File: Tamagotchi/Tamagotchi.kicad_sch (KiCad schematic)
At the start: 1 part, among them U1 XIAO-ESP32-C6-DIP

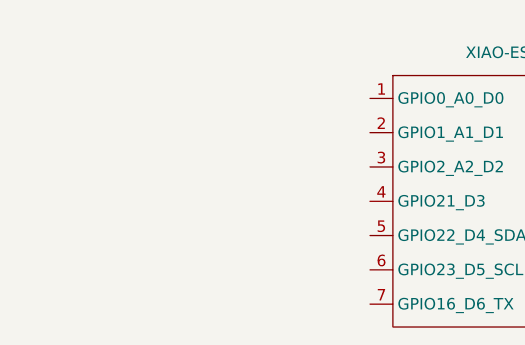
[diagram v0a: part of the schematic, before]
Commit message: finally found a oled
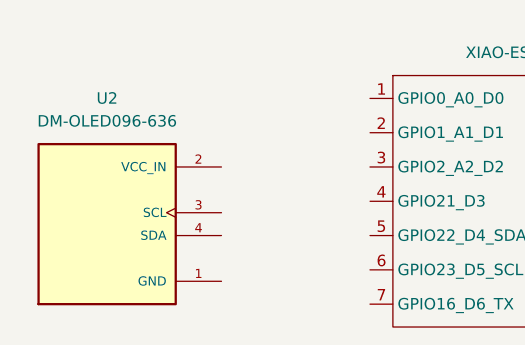
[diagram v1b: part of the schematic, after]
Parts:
- added U2: DM-OLED096-636, DM-OLED096-636:MODULE_DM-OLED096-636, symbol DM-OLED096-636:DM-OLED096-636
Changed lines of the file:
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@@
 	(paper "A4")
+	(symbol
+		(lib_id "DM-OLED096-636:DM-OLED096-636")
+		(at 100.33 95.25 0)
+		(unit 1)
+		(body_style 1)
+		(exclude_from_sim no)
+		(in_bom yes)
+		(on_board yes)
+		(in_pos_files yes)
+		(dnp no)
+		(fields_autoplaced yes)
+		(property "Reference" "U2"
+			(at 100.33 80.01 0)
+			(show_name no)
+			(do_not_autoplace no)
+			(effects
+				(font
+					(size 1.27 1.27)
+				)
+			)
+		)
+		(property "Value" "DM-OLED096-636"
+			(at 100.33 82.55 0)
+			(show_name no)
+			(do_not_autoplace no)
+			(effects
+				(font
+					(size 1.27 1.27)
+				)
+			)
+		)
+		(property "Footprint" "DM-OLED096-636:MODULE_DM-OLED096-636"
+			(at 100.33 95.25 0)
+			(hide yes)
+			(show_name no)
+			(do_not_autoplace no)
+			(effects
+				(font
+					(size 1.27 1.27)
+				)
+				(justify bottom)
+			)
+		)
+		(property "Datasheet" ""
+			(at 100.33 95.25 0)
+			(hide yes)
+			(show_name no)
+			(do_not_autoplace no)
+			(effects
+				(font
+					(size 1.27 1.27)
+				)
+			)
+		)
+		(property "Description" "0.96” 128 X 64 MONOCHROME GRAPHIC OLED DISPLAY MODULE - I2C"
+			(at 100.33 95.25 0)
+			(hide yes)
+			(show_name no)
+			(do_not_autoplace no)
+			(effects
+				(font
+					(size 1.27 1.27)
+				)
+				(justify bottom)
+			)
+		)
+		(property "MF" "Display Module"
+			(at 100.33 95.25 0)
+			(hide yes)
+			(show_name no)
+			(do_not_autoplace no)
+			(effects
+				(font
+					(size 1.27 1.27)
+				)
+				(justify bottom)
+			)
+		)
+		(property "MAXIMUM_PACKAGE_HEIGHT" "11.3 mm"
+			(at 100.33 95.25 0)
+			(hide yes)
+			(show_name no)
+			(do_not_autoplace no)
+			(effects
+				(font
+					(size 1.27 1.27)
+				)
+				(justify bottom)
+			)
+		)
+		(property "Package" "Package"
+			(at 100.33 95.25 0)
+			(hide yes)
+			(show_name no)
+			(do_not_autoplace no)
+			(effects
+				(font
+					(size 1.27 1.27)
+				)
+				(justify bottom)
+			)
+		)
+		(property "Price" "None"
+			(at 100.33 95.25 0)
+			(hide yes)
+			(show_name no)
+			(do_not_autoplace no)
+			(effects
+				(font
+					(size 1.27 1.27)
+				)
+				(justify bottom)
+			)
+		)
+		(property "Check_prices" "https://www.snapeda.com/parts/DM-OLED096-636/Display+Module/view-part/?ref=eda"
+			(at 100.33 95.25 0)
+			(hide yes)
+			(show_name no)
+			(do_not_autoplace no)
+			(effects
+				(font
+					(size 1.27 1.27)
+				)
+				(justify bottom)
+			)
+		)
+		(property "STANDARD" "Manufacturer Recommendations"
+			(at 100.33 95.25 0)
+			(hide yes)
+			(show_name no)
+			(do_not_autoplace no)
+			(effects
+				(font
+					(size 1.27 1.27)
+				)
+				(justify bottom)
+			)
+		)
+		(property "PARTREV" "2018-09-10"
+			(at 100.33 95.25 0)
+			(hide yes)
+			(show_name no)
+			(do_not_autoplace no)
+			(effects
+				(font
+					(size 1.27 1.27)
+				)
+				(justify bottom)
+			)
+		)
+		(property "SnapEDA_Link" "https://www.snapeda.com/parts/DM-OLED096-636/Display+Module/view-part/?ref=snap"
+			(at 100.33 95.25 0)
+			(hide yes)
+			(show_name no)
+			(do_not_autoplace no)
+			(effects
+				(font
+					(size 1.27 1.27)
+				)
+				(justify bottom)
+			)
+		)
+		(property "MP" "DM-OLED096-636"
+			(at 100.33 95.25 0)
+			(hide yes)
+			(show_name no)
+			(do_not_autoplace no)
+			(effects
+				(font
+					(size 1.27 1.27)
+				)
+				(justify bottom)
+			)
+		)
+		(property "Availability" "Not in stock"
+			(at 100.33 95.25 0)
+			(hide yes)
+			(show_name no)
+			(do_not_autoplace no)
+			(effects
+				(font
+					(size 1.27 1.27)
+				)
+				(justify bottom)
+			)
+		)
+		(property "MANUFACTURER" "Displaymodule"
+			(at 100.33 95.25 0)
+			(hide yes)
+			(show_name no)
+			(do_not_autoplace no)
+			(effects
+				(font
+					(size 1.27 1.27)
+				)
+				(justify bottom)
+			)
+		)
+		(pin "4"
+		)
+		(pin "3"
+		)
+		(pin "1"
+		)
+		(pin "2"
+		)
+		(instances
+			(project "Tamagotchi"
+				(path "/dd5d29a8-0ca1-4c75-a105-470d6b907a46"
+					(reference "U2")
+					(unit 1)
+				)
+			)
+		)
+	)
 	(symbol
 		(lib_id "Seeed_Studio_XIAO_Series:XIAO-ESP32-C6-DIP")

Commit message: finished the schematic
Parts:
- added D1, D2, D3: LED, LED_THT:LED_D1.8mm_W1.8mm_H2.4mm_Horizontal_O1.27mm_Z4.9mm, symbol Device:LED
- added SW1, SW2, SW3: SW_Push, Button_Switch_THT:KSA_Tactile_SPST, symbol Switch:SW_Push
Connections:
- net GND: now reaches U2.1 (GND)
- net GND: now also U1.13 (GND), D1.1 (K), D2.1 (K), D3.1 (K), SW1.1, SW2.1, SW3.1
- net +3V3: now reaches U2.2 (VCC_IN)
- net +3V3: now also U1.12 (3V3)
- net at U2.3 (SCL): now also U1.6 (GPIO23_D5_SCL)
- net at U2.4 (SDA): now also U1.5 (GPIO22_D4_SDA)
- net at U1.1 (GPIO0_A0_D0): now also SW1.2
- net +5V: now reaches U1.14 (VBUS)
- net at U1.2 (GPIO1_A1_D1): now also SW2.2
- net at U1.3 (GPIO2_A2_D2): now also SW3.2
- net at U1.4 (GPIO21_D3): now also D1.2 (A)
- net at U1.7 (GPIO16_D6_TX): now also D3.2 (A)
- net at U1.8 (GPIO17_D7_RX): now also D2.2 (A)

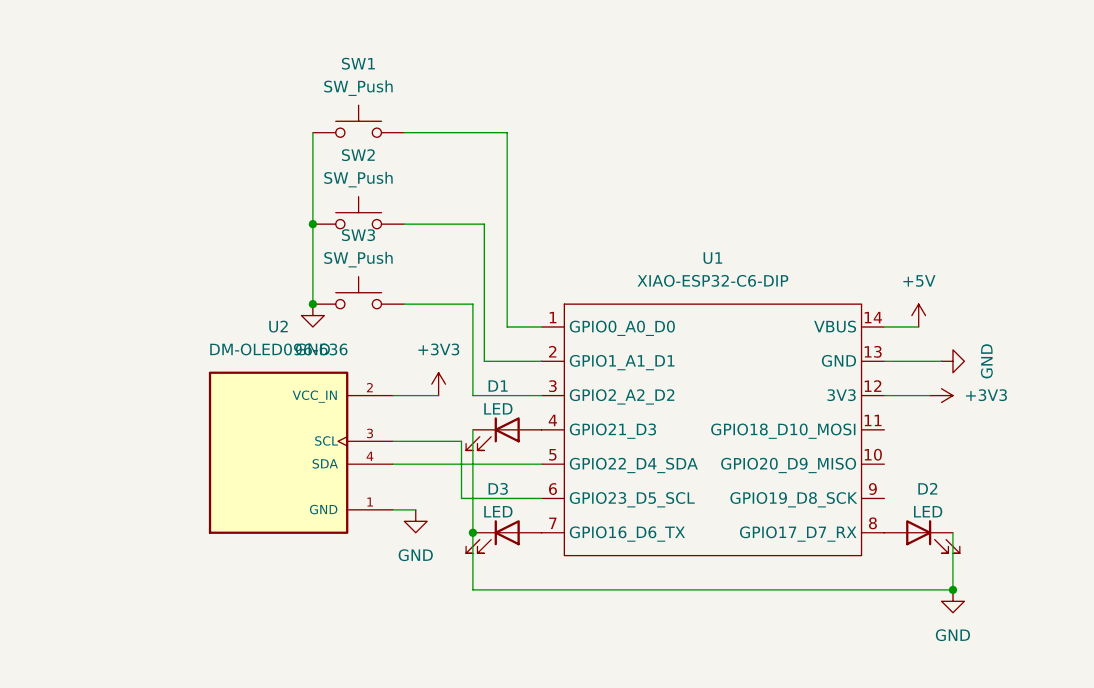
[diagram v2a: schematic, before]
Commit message: trying to fix my errors in schematic
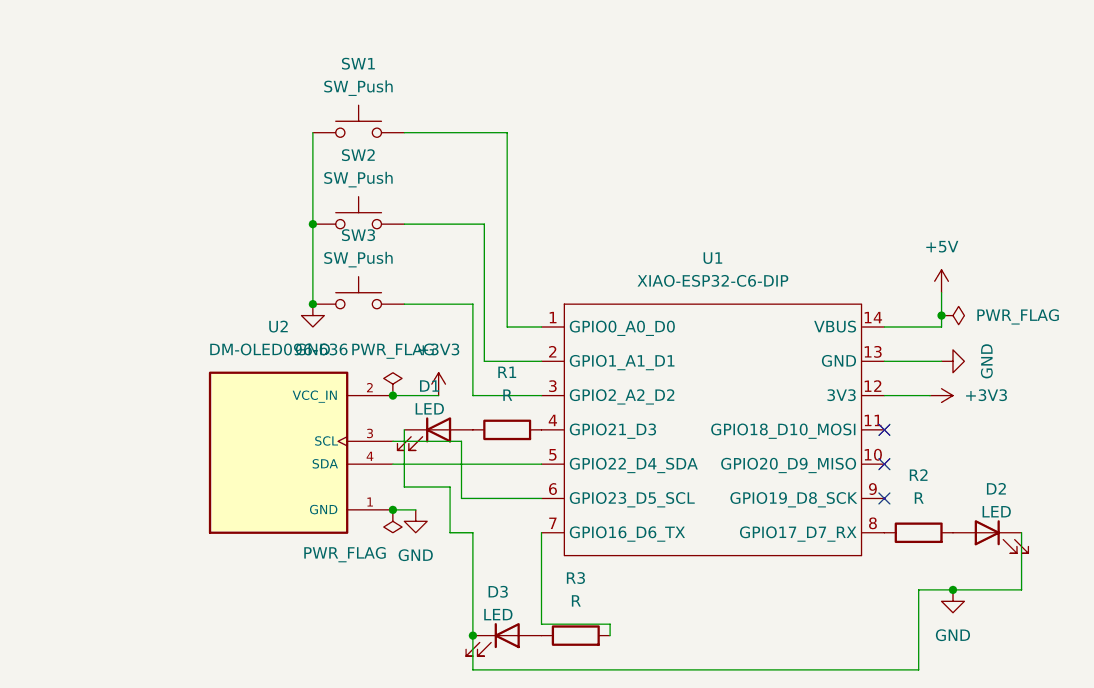
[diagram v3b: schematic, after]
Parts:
- added R1, R2, R3: R, symbol Device:R
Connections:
- net at D1.2 (A): now also R1.1; no longer U1.4 (GPIO21_D3)
- net at D3.2 (A): now also R3.1; no longer U1.7 (GPIO16_D6_TX)
- net at U1.8 (GPIO17_D7_RX): now also R2.1; no longer D2.2 (A)
- new net: R3.2, U1.7 (GPIO16_D6_TX)
- new net: R1.2, U1.4 (GPIO21_D3)
- new net: D2.2 (A), R2.2
- no-connect marks 0 -> 3
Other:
- moved on the sheet: D1, D2, D3

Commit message: spend so much time finding footprints
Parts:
- R1, R2, R3: footprint (none) -> Resistor_THT:R_Axial_DIN0204_L3.6mm_D1.6mm_P5.08mm_Horizontal
- U1: footprint Seeed_Studio_XIAO_Series:XIAO-ESP32-C6-DIP -> Seeed Studio XIAO Series Library:XIAO-ESP32-C6-DIP
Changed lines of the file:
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@@
 			)
 		)
-		(property "Footprint" ""
+		(property "Footprint" "Resistor_THT:R_Axial_DIN0204_L3.6mm_D1.6mm_P5.08mm_Horizontal"
 			(at 133.35 116.078 90)
 			(hide yes)
@@
 			)
 		)
-		(property "Footprint" ""
+		(property "Footprint" "Resistor_THT:R_Axial_DIN0204_L3.6mm_D1.6mm_P5.08mm_Horizontal"
 			(at 125.73 93.218 90)
 			(hide yes)
@@
 			)
 		)
-		(property "Footprint" "Seeed_Studio_XIAO_Series:XIAO-ESP32-C6-DIP"
+		(property "Footprint" "Seeed Studio XIAO Series Library:XIAO-ESP32-C6-DIP"
 			(at 149.86 86.36 0)
 			(hide yes)
@@
 			)
 		)
-		(property "Footprint" ""
+		(property "Footprint" "Resistor_THT:R_Axial_DIN0204_L3.6mm_D1.6mm_P5.08mm_Horizontal"
 			(at 171.45 104.648 90)
 			(hide yes)

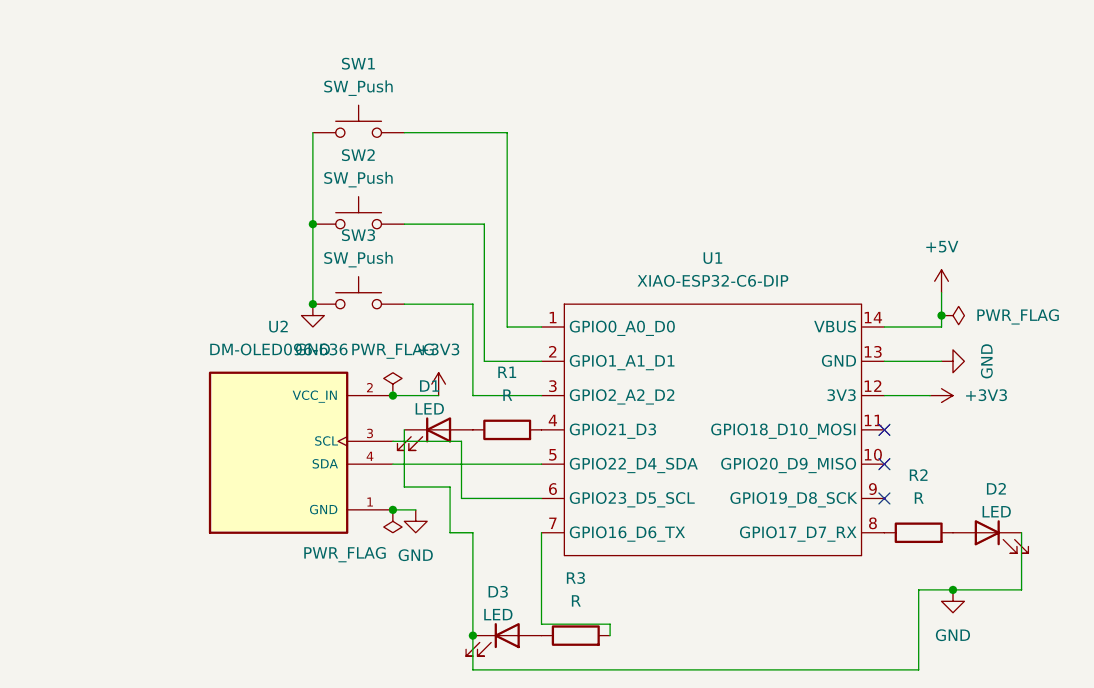
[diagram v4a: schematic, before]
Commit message: added some resistor and capacitors
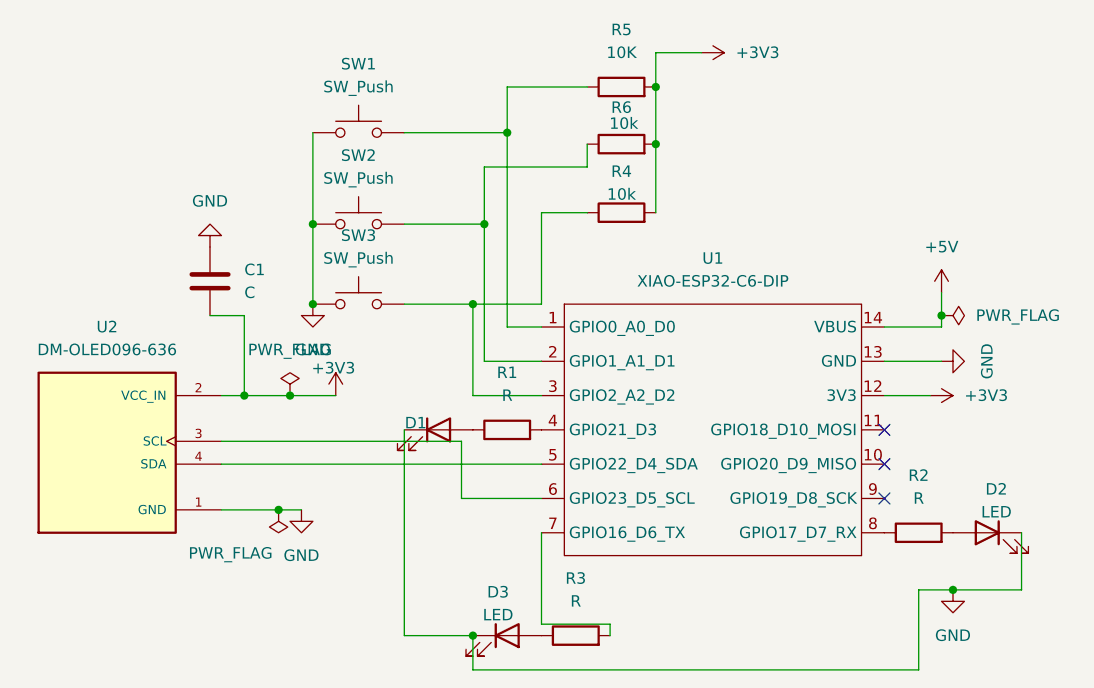
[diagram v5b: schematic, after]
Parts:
- added C1: C, Capacitor_SMD:C_0805_2012Metric, symbol Device:C
- added R4, R6: 10k, Resistor_SMD:R_0805_2012Metric, symbol Device:R
- added R5: 10K, Resistor_SMD:R_0805_2012Metric, symbol Device:R
- R1, R2, R3: footprint Resistor_THT:R_Axial_DIN0204_L3.6mm_D1.6mm_P5.08mm_Horizontal -> Resistor_SMD:R_0805_2012Metric
- U2: footprint DM-OLED096-636:MODULE_DM-OLED096-636 -> DM-OLED096-636 (1):MODULE_DM-OLED096-636
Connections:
- net +3V3: now also C1.1, R4.2, R5.2, R6.2
- net GND: now also C1.2
- net at SW1.2, U1.1 (GPIO0_A0_D0): now also R5.1
- net at SW2.2, U1.2 (GPIO1_A1_D1): now also R6.1
- net at SW3.2, U1.3 (GPIO2_A2_D2): now also R4.1
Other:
- moved on the sheet: U2

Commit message: made sme step file to use for the case modeling
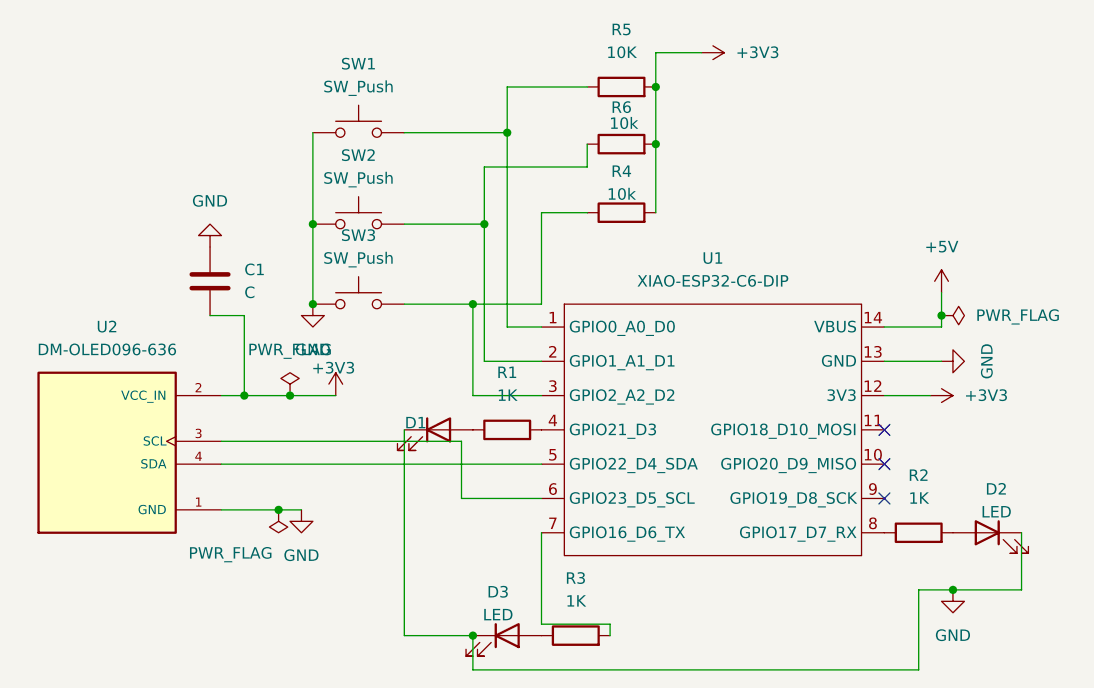
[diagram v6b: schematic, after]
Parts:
- R1, R2, R3: value R -> 1K
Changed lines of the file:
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@@
 			)
 		)
-		(property "Value" "R"
+		(property "Value" "1K"
 			(at 133.35 110.49 90)
 			(show_name no)
@@
 			)
 		)
-		(property "Value" "R"
+		(property "Value" "1K"
 			(at 125.73 87.63 90)
 			(show_name no)
@@
 			)
 		)
-		(property "Value" "R"
+		(property "Value" "1K"
 			(at 171.45 99.06 90)
 			(show_name no)
